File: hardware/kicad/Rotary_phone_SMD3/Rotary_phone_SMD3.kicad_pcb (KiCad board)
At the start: 2 copper layers, 100 x 50 mm, 72 parts, among them J1 Barrel_Jack_PTH_Slot, J10 RJ12, J11 PINHD_1x2_Male, J2 PINHD_1x2_Male, J3 PINHD_1x2_Male, J4 PINHD_1x2_Male, J5 PINHD_1x2_Male, J6 PINHD_1x2_Male, J7 PINHD_1x2_Male, J8 PINHD_1x2_Male, J9 RJ12, U1 ME6211C33M5G-N, U2 ESP32-C6-WROOM-1, U3 USBLC6-2SC6, U4 ES8388, U5 AG1171, U6 AG1171

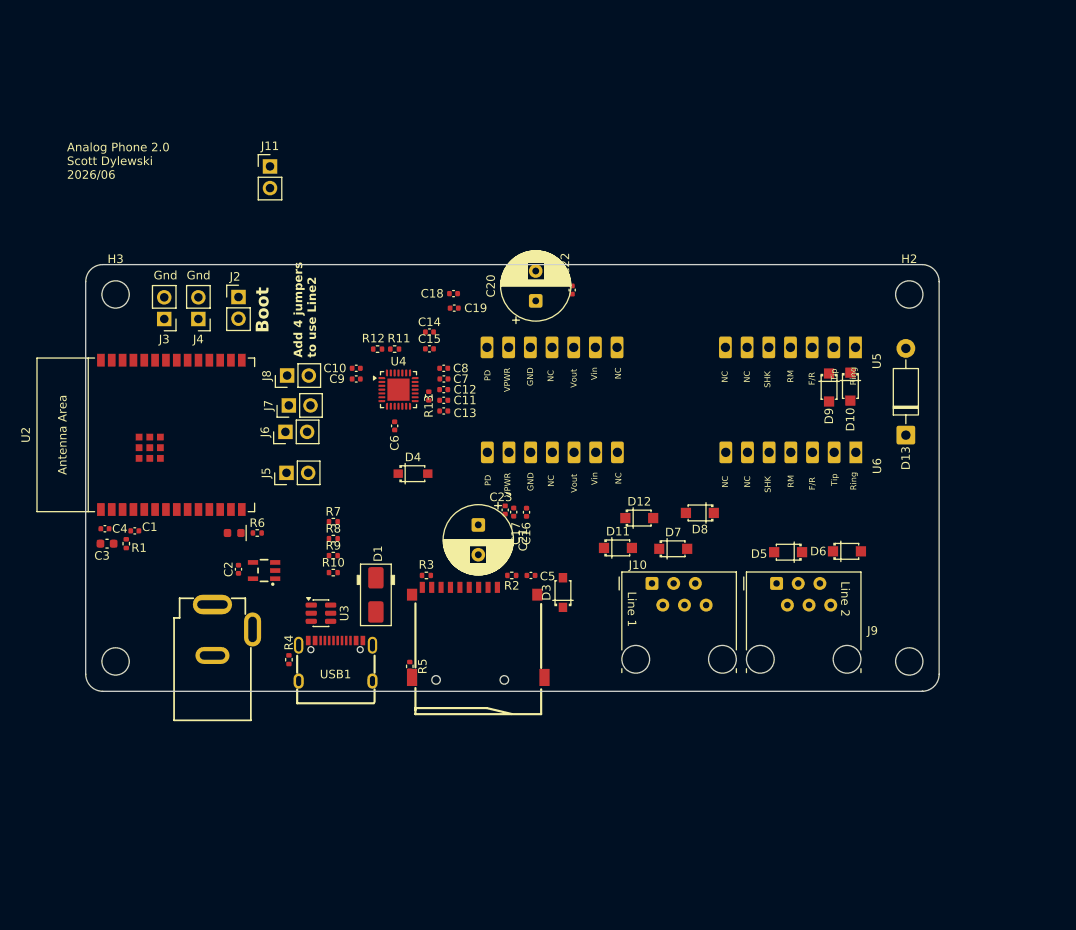
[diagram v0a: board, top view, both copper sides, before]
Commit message: 211 recording rework, activity log, ag1170 pulse-debounce fix, SMD4 board, public docs pass
Firmware:
- ag1170: require a minimum loop-open duration (pulse_break_min_ms=15) for a
  rotary pulse to count, not just a maximum -- fixes a ~3-5ms mechanical
  contact-bounce glitch occasionally being miscounted as an extra pulse
  (confirmed live: "211" misread as "212"/"322").
- 211 recording: drop the escalating warning-beep sequence in favor of just
  ending the recording silently; default max length raised 30s -> 2min
  (still user-adjustable, capped at BOARD_RECORD_MAX_MS_MAX); recorder AGC
  with a per-block hard ceiling to stop a startup transient from clipping;
  8s trailing-silence auto-stop kept from the previous tuning pass.
- Recordings/storage lists now sort newest-first.
- sdcard: optional card-detect (CD) pin support, wired up for SMD4 (inert on
  boards without BOARD_SD_CD defined).
- New `activity` component: small ring buffer of human-readable recent
  events (calls, recordings, dial errors) for the Status page, independent
  of the raw debug log.
- webui: dial-code/guide cards moved onto the Status page; the raw debug log
  panel moved to the Diagnostics tab (Settings), next to the log-level
  controls it belongs with.
- voip: retire the voip_provisioner auto-provisioning companion service in
  favor of a plain per-board setup password (gates /api/prompt_requests for
  gen_prompt.py --sync); ships with no default SIP server/hostname baked in.
- dialplan: drop four novelty dial-code clips whose source audio never
  shipped in this checkout (burp/dial-up modem remain).

Hardware:
- Add the SMD4 KiCad project (SMD3's schematic re-routed as a 2-layer
  board); add a 3d-printed-case doc stub.
- Drop SMD3's fab-output cruft (gerbers, DRC/ERC reports, JLCImport
  libraries, BOM) from tracking -- regenerable, and JLCImport in particular
  carries machine-local absolute paths. .gitignore now covers this class of
  file for every board going forward instead of one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
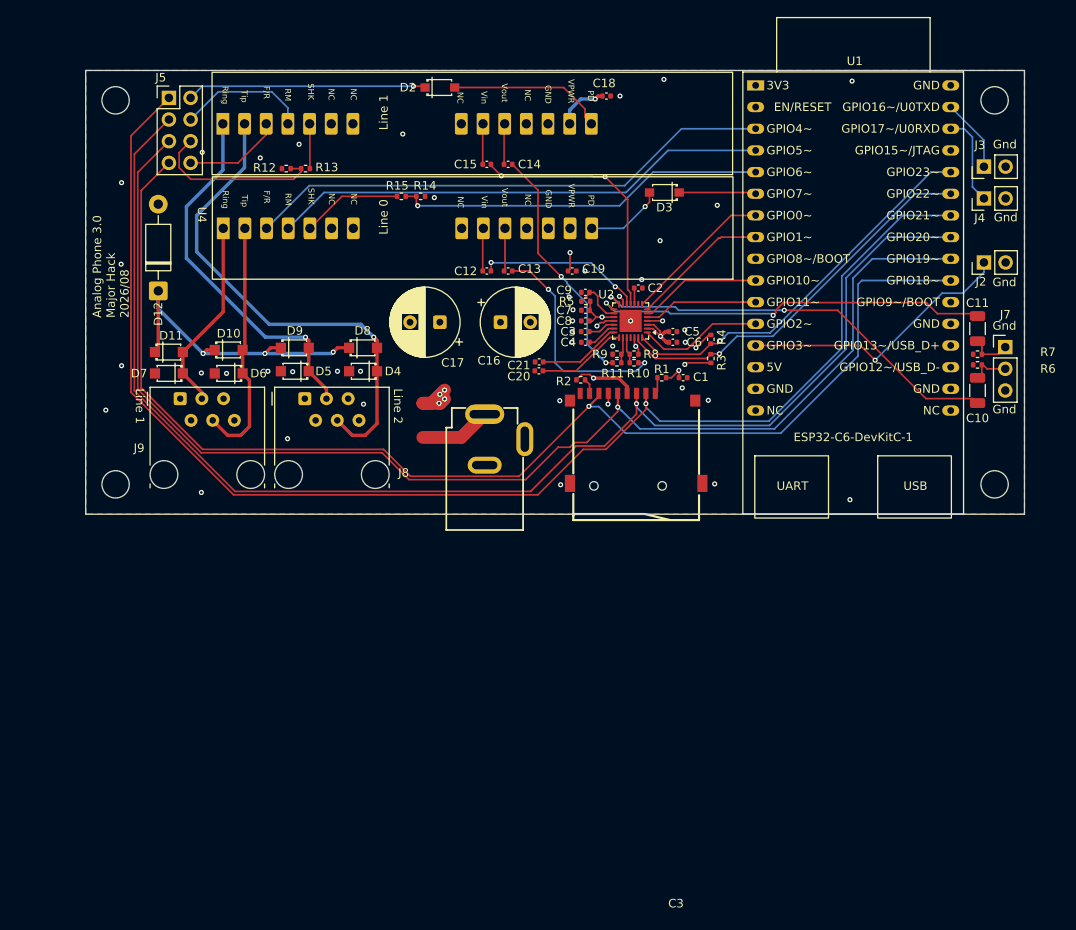
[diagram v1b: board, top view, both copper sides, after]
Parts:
- removed the C1 at (55.8, 104.0)
- removed the C2 at (67.9, 108.5)
- removed the C3 at (52.5, 105.5)
- removed the C4 at (52.2, 103.7)
- removed D1: SS14, PCM_Diode_SMD_AKL:D_SMA
- removed the D2 at (67.4, 104.2)
- removed J11, J6: PINHD_1x2_Male, Connector_PinHeader_2.54mm:PinHeader_1x02_P2.54mm_Vertical
- removed the J8 at (73.6, 85.8)
- removed the R1 at (54.8, 105.5)
- removed the R4 at (73.8, 119.0)
- removed the R5 at (88.0, 119.8)
- removed the U2 at (60.0, 92.7)
- removed the U3 at (77.6, 113.6)
- removed USB1: TYPE-C_16PIN_2MD_073, JLCImport:TYPE-C_16PIN_2MD_073
- added C20: 100nF, Capacitor_SMD:C_0402_1005Metric, F.Cu at (103.1, 85.2)
- added C21: 100nF, Capacitor_SMD:C_0402_1005Metric, F.Cu at (103.1, 84.2)
- added R10: 10k, Resistor_SMD:R_0402_1005Metric, F.Cu at (114.2, 84.2)
- added R11: 10k, Resistor_SMD:R_0402_1005Metric, F.Cu at (112.2, 84.2)
- added R7: 47k, Resistor_SMD:R_0402_1005Metric, F.Cu at (154.5, 83.2)
- added R8: 8.2k, Resistor_SMD:R_0402_1005Metric, F.Cu at (114.2, 83.2)
- added R9: 8.2k, Resistor_SMD:R_0402_1005Metric, F.Cu at (112.2, 83.2)
- C10: renamed from C14; value 100nF -> 100uF; footprint Capacitor_SMD:C_0402_1005Metric -> Capacitor_SMD:C_1206_3216Metric
- C11: renamed from C15; value 100nF -> 100uF; footprint Capacitor_SMD:C_0402_1005Metric -> Capacitor_SMD:C_1206_3216Metric
- J5: value PINHD_1x2_Male -> PINHD_2x4_Male; footprint Connector_PinHeader_2.54mm:PinHeader_1x02_P2.54mm_Vertical -> Connector_PinHeader_2.54mm:PinHeader_2x04_P2.54mm_Vertical
- J7: value PINHD_1x2_Male -> PINHD_1x3_Male; footprint Connector_PinHeader_2.54mm:PinHeader_1x02_P2.54mm_Vertical -> Connector_PinHeader_2.54mm:PinHeader_1x03_P2.54mm_Vertical
- R6: value 220R -> 47k
- U1: value ME6211C33M5G-N -> ESP32-C6-DevKitC-1; footprint PCM_SparkFun-Semiconductor-Standard:SOT23-5 -> PCM_Espressif:ESP32-C6-DevKitC-1
- moved J3 97.7 mm to (155.2, 61.3), turned to 90 degrees
- moved J4 93.1 mm to (155.2, 65.0), turned to 90 degrees
- moved D12 89.2 mm to (58.5, 75.8)
- moved J2 87.4 mm to (155.2, 72.5), turned to 90 degrees
- moved R6 86.7 mm to (154.5, 84.5)
- moved J7 84.2 mm to (157.8, 82.4), turned to 0 degrees
- moved U1 80.9 mm to (128.5, 51.8), turned to 0 degrees
- moved D5 68.1 mm to (74.5, 85.2), turned to 180 degrees
- moved D9 65.3 mm to (74.5, 82.5), turned to 0 degrees
- moved C10 64.6 mm to (154.5, 87.5), turned to -90 degrees
- moved D7 64.3 mm to (59.8, 85.5)
- moved C11 64.3 mm to (154.5, 80.2), turned to 90 degrees
- moved D2 60.9 mm to (91.5, 52.0), turned to 0 degrees
- moved J9 59.4 mm to (61.1, 88.5)
- moved J8 59.4 mm to (75.7, 88.5)
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- renumbered C5 to C1, C16 to C12, C17 to C13, C18 to C14, C19 to C15, C20 to C16, C21 to C17, C22 to C18, C23 to C19, C6 to C2, C7 to C3, C8 to C4, C9 to C5, C10 to C6, C11 to C7, C12 to C8, C13 to C9, D11 to D10, D12 to D11, D13 to D12, D3 to D2, D4 to D3, D5 to D4, D6 to D5, D7 to D6, D8 to D7, D9 to D8, D10 to D9, J9 to J8, J10 to J9, R2 to R1, R10 to R12, R11 to R13, R12 to R14, R13 to R15, R3 to R2, R7 to R3, R8 to R4, R9 to R5, U4 to U2, U5 to U3, U6 to U4
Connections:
- net /Line1_Vin renamed /CH0_Spk
- net /Line2_Vin renamed /CH1_Spk
- C10 pad 1: GND -> Net-(C10-Pad1)
- C10 pad 2: Net-(U4-RIN1) -> Net-(U2-ROUT2)
- C11 pad 1: GND -> Net-(C11-Pad1)
- C11 pad 2: Net-(U4-RIN2) -> Net-(U2-LOUT2)
- C13 pad 1: /Line1_Vout -> /CH0_Mic
- C14 pad 2: /Line2_Vout -> /CH1_Mic
- D10 pad 2: Net-(D11-A) -> /Line1Tip
- D11 pad 2: Net-(D12-A) -> /Line1Ring
- D2 pad 1: /Line2_PD -> /Line1_PD
- D3 pad 1: /Line1_PD -> /Line0_PD
- D4 pad 1: Net-(D5-K) -> /Line2Tip
- D5 pad 1: Net-(D10-A) -> /Line2Ring
- D6 pad 1: Net-(D11-A) -> /Line1Tip
- D7 pad 1: Net-(D12-A) -> /Line1Ring
- D8 pad 2: Net-(D5-K) -> /Line2Tip
- D9 pad 2: Net-(D10-A) -> /Line2Ring
- J1 pad PWR: +5V -> Net-(D1-A)
- J2 pad 1: Net-(U2-GPIO9) -> /Xtra1
- J3 pad 1: Net-(U2-U0TXD/GPIO16) -> Net-(U1-GPIO16/U0TXD)
- J4 pad 1: Net-(U2-U0RXD/GPIO17) -> Net-(U1-GPIO17/U0RXD)
- J5 pad 2: /Line2_PD -> /Line1_PD
- J7 pad 1: /SD_MOSI -> Net-(C11-Pad1)
- J7 pad 2: /Line2_RM -> Net-(C10-Pad1)
- J8 pad 3: Net-(D5-K) -> /Line2Ring
- J8 pad 4: Net-(D10-A) -> /Line2Tip
- J9 pad 3: Net-(D11-A) -> /Line1Ring
- J9 pad 4: Net-(D12-A) -> /Line1Tip
- R12 pad 2: /Line2_SHK -> /Line1_SHK
- R13 pad 1: /Line2_SHK -> /Line1_SHK
- R14 pad 2: /Line1_SHK -> /Line0_SHK
- R15 pad 1: /Line1_SHK -> /Line0_SHK
- R6 pad 1: Net-(D2-K) -> GND
- R6 pad 2: GND -> Net-(C10-Pad1)
- U1 pad 1: +5V -> +3.3V
- U1 pad 2: GND -> unconnected-(U1-EN/RESET-Pad2)
- U1 pad 3: +5V -> /Line0_F/R
- U1 pad 4: unconnected-(U1-NC-Pad4) -> /Line0_RM
- U1 pad 5: +3.3V -> /Line0_SHK
- U2 pad 14: unconnected-(U4-ROUT2-Pad14) -> Net-(U2-ROUT2)
- U2 pad 15: unconnected-(U4-LOUT2-Pad15) -> Net-(U2-LOUT2)
- U2 pad 21: Net-(U4-RIN2) -> Net-(U2-RIN2)
- U2 pad 22: /Line2_Vout -> Net-(U2-LIN2)
- U2 pad 23: Net-(U4-RIN1) -> Net-(U2-RIN1)
- U2 pad 24: /Line1_Vout -> Net-(U2-LIN1)
- U3 pad 1: Net-(D10-A) -> /Line2Ring
- U3 pad 2: Net-(D5-K) -> /Line2Tip
- U3 pad 3: /Line2_F/R -> /Line1_F/R
- U3 pad 4: /Line2_RM -> /Line1_RM
- U4 pad 1: Net-(D12-A) -> /Line1Ring
- U4 pad 2: Net-(D11-A) -> /Line1Tip
- U4 pad 3: /Line1_F/R -> /Line0_F/R
- U4 pad 4: /Line1_RM -> /Line0_RM
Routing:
- net /SD_CS: track 0.00 -> 160.6 mm, vias 0 -> 1
- net /SD_MOSI: track 0.00 -> 155.5 mm, vias 0 -> 1
- net /SD_CLK: track 0.00 -> 151.5 mm, vias 0 -> 1
- net /SD_MISO: track 0.00 -> 147.6 mm, vias 0 -> 1
- net +5V: track 0.00 -> 125.1 mm, vias 0 -> 6
- net +3.3V: track 0.00 -> 88.6 mm, vias 0 -> 6
- net /Line0_F/R: track 0.00 -> 62.1 mm
- net /Line0_RM: track 0.00 -> 58.6 mm
- net /Line2Tip: track 0.00 -> 58.5 mm, vias 0 -> 1
- net Net-(U2-ROUT2): track 0.00 -> 49.4 mm, vias 0 -> 2
- net Net-(U2-LOUT2): track 0.00 -> 46.8 mm, vias 0 -> 2
- net /I2C_SDA: track 0.00 -> 45.9 mm, vias 0 -> 1
- net /I2C_SCL: track 0.00 -> 45.8 mm, vias 0 -> 1
- net /Line0_SHK: track 0.00 -> 43.6 mm, vias 0 -> 1
- net /Line2Ring: track 0.00 -> 43.5 mm, vias 0 -> 1
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- added copper zone on F.Cu, net GND
- added copper zone on In2.Cu, net GND
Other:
- board size 100 x 50 mm -> 110 x 52 mm
- copper layers 2 -> 4
- board text added: "Analog Phone 3.0 Major Hack 2026/08"
- board text added: "Line 0"
- board text removed: "Add 4 jumpers to use Line2"
- board text removed: "Analog Phone 2.0 Scott Dylewski 2026/06"
- board text removed: "Boot"

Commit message: kicad: consolidate custom footprints/3D/symbols into libraries/
Move all per-project Scott.pretty, JLCImport.pretty, .3dshapes, and
.kicad_sym files into a single shared kicad/libraries/ directory.
Rename "Scott" library to "Custom" throughout. Update fp-lib-table,
sym-lib-table, .kicad_pcb, and .kicad_sch files in all 6 board
projects to resolve Custom: and JLCImport: via ${KIPRJMOD}/../libraries/.

Also fixes broken 3D model paths (hardcoded /Users/... and
_restore_backup_ references in SMD3/SMD4/AR5 PCBs).

Generated with [Devin](https://devin.ai)

Co-Authored-By: Devin <158243242+devin-ai-integration[bot]@users.noreply.github.com>
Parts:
- J8, J9: footprint Scott:RJ12_Amphenol_87180_Horizontal -> Custom:RJ12_Amphenol_87180_Horizontal
- U3, U4: footprint Scott:AG1171_SIL -> Custom:AG1171_SIL
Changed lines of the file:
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@@
 		)
 	)
-	(footprint "Scott:AG1171_SIL"
+	(footprint "Custom:AG1171_SIL"
 		(locked yes)
 		(layer "F.Cu")
@@
 		)
 		(embedded_fonts no)
-		(model "${KIPRJMOD}/Scott.3dshapes/AG1171.step"
+		(model "${KIPRJMOD}/../libraries/Custom.3dshapes/AG1171.step"
 			(offset
 				(xyz 31.25 4.3 0)
@@
 		)
 		(embedded_fonts no)
-		(model "${KIPRJMOD}/_restore_backup_2026-08-30T20-24-25-026/JLCImport.3dshapes/1N4007W_C18199088.step"
+		(model "${KIPRJMOD}/../libraries/JLCImport.3dshapes/1N4007W_C18199088.step"
 			(offset
 				(xyz 0 0 -0.09)
@@
 		)
 		(embedded_fonts no)
-		(model "${KIPRJMOD}/_restore_backup_2026-08-30T20-24-25-026/JLCImport.3dshapes/TF-01A.step"
+		(model "${KIPRJMOD}/../libraries/JLCImport.3dshapes/TF-01A.step"
 			(offset
 				(xyz 0.002223 -5.10134 0.14732)
@@
 		)
 	)
-	(footprint "Scott:RJ12_Amphenol_87180_Horizontal"
+	(footprint "Custom:RJ12_Amphenol_87180_Horizontal"
 		(layer "F.Cu")
 		(at 61.07 88.46)
@@
 		)
 		(embedded_fonts no)
-		(model "${KIPRJMOD}/Scott.3dshapes/87180-066LF.step"
+		(model "${KIPRJMOD}/../libraries/Custom.3dshapes/87180-066LF.step"
 			(offset
 				(xyz 0 0 0)
@@
 		)
 		(embedded_fonts no)
-		(model "${KIPRJMOD}/_restore_backup_2026-08-30T20-24-25-026/JLCImport.3dshapes/1N4148W_C81598.step"
+		(model "${KIPRJMOD}/../libraries/JLCImport.3dshapes/1N4148W_C81598.step"
 			(offset
 				(xyz 0 0 0)
@@
 		)
 		(embedded_fonts no)
-		(model "${KIPRJMOD}/_restore_backup_2026-08-30T20-24-25-026/JLCImport.3dshapes/1N4007W_C18199088.step"
+		(model "${KIPRJMOD}/../libraries/JLCImport.3dshapes/1N4007W_C18199088.step"
 			(offset
 				(xyz 0 0 -0.09)
@@
 		)
 		(embedded_fonts no)
-		(model "${KIPRJMOD}/_restore_backup_2026-08-30T20-24-25-026/JLCImport.3dshapes/1N4007W_C18199088.step"
+		(model "${KIPRJMOD}/../libraries/JLCImport.3dshapes/1N4007W_C18199088.step"
 			(offset
 				(xyz 0 0 -0.09)
@@
 		)
 		(embedded_fonts no)
-		(model "${KIPRJMOD}/_restore_backup_2026-08-30T20-24-25-026/JLCImport.3dshapes/1N4007W_C18199088.step"
+		(model "${KIPRJMOD}/../libraries/JLCImport.3dshapes/1N4007W_C18199088.step"
 			(offset
 				(xyz 0 0 -0.09)
@@
 		)
 	)
-	(footprint "Scott:AG1171_SIL"
+	(footprint "Custom:AG1171_SIL"
 		(locked yes)
 		(layer "F.Cu")
@@
 		)
 		(embedded_fonts no)
-		(model "${KIPRJMOD}/Scott.3dshapes/AG1171.step"
+		(model "${KIPRJMOD}/../libraries/Custom.3dshapes/AG1171.step"
 			(offset
 				(xyz 31.25 4.3 0)
@@
 		)
 		(embedded_fonts no)
-		(model "${KIPRJMOD}/_restore_backup_2026-08-30T20-24-25-026/JLCImport.3dshapes/1N4007W_C18199088.step"
+		(model "${KIPRJMOD}/../libraries/JLCImport.3dshapes/1N4007W_C18199088.step"
 			(offset
 				(xyz 0 0 -0.09)
@@
 		)
 		(embedded_fonts no)
-		(model "${KIPRJMOD}/_restore_backup_2026-08-30T20-24-25-026/JLCImport.3dshapes/1N4007W_C18199088.step"
+		(model "${KIPRJMOD}/../libraries/JLCImport.3dshapes/1N4007W_C18199088.step"
 			(offset
 				(xyz 0 0 -0.09)
@@
 		)
 		(embedded_fonts no)
-		(model "${KIPRJMOD}/_restore_backup_2026-08-30T20-24-25-026/JLCImport.3dshapes/1N4007W_C18199088.step"
+		(model "${KIPRJMOD}/../libraries/JLCImport.3dshapes/1N4007W_C18199088.step"
 			(offset
 				(xyz 0 0 -0.09)
@@
 		)
 	)
-	(footprint "Scott:RJ12_Amphenol_87180_Horizontal"
+	(footprint "Custom:RJ12_Amphenol_87180_Horizontal"
 		(layer "F.Cu")
 		(at 75.67 88.46)
@@
 		)
 		(embedded_fonts no)
-		(model "${KIPRJMOD}/Scott.3dshapes/87180-066LF.step"
+		(model "${KIPRJMOD}/../libraries/Custom.3dshapes/87180-066LF.step"
 			(offset
 				(xyz 0 0 0)
@@
 		)
 		(embedded_fonts no)
-		(model "${KIPRJMOD}/_restore_backup_2026-08-30T20-24-25-026/JLCImport.3dshapes/1N4148W_C81598.step"
+		(model "${KIPRJMOD}/../libraries/JLCImport.3dshapes/1N4148W_C81598.step"
 			(offset
 				(xyz 0 0 0)
@@
 		)
 		(embedded_fonts no)
-		(model "${KIPRJMOD}/_restore_backup_2026-08-30T20-24-25-026/JLCImport.3dshapes/1N4007W_C18199088.step"
+		(model "${KIPRJMOD}/../libraries/JLCImport.3dshapes/1N4007W_C18199088.step"
 			(offset
 				(xyz 0 0 -0.09)
